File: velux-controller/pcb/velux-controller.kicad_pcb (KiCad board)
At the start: 2 copper layers, 69.9 x 69.8 mm, 35 parts, among them J1 UART, J2 POWER, J3 SIGNAL, J4 PWR, Q1 MMBT3904, Q2 MMBT3904, Q3 MMBT3904, SW1 BOOT, SW2 RST, U1 ESP-12F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

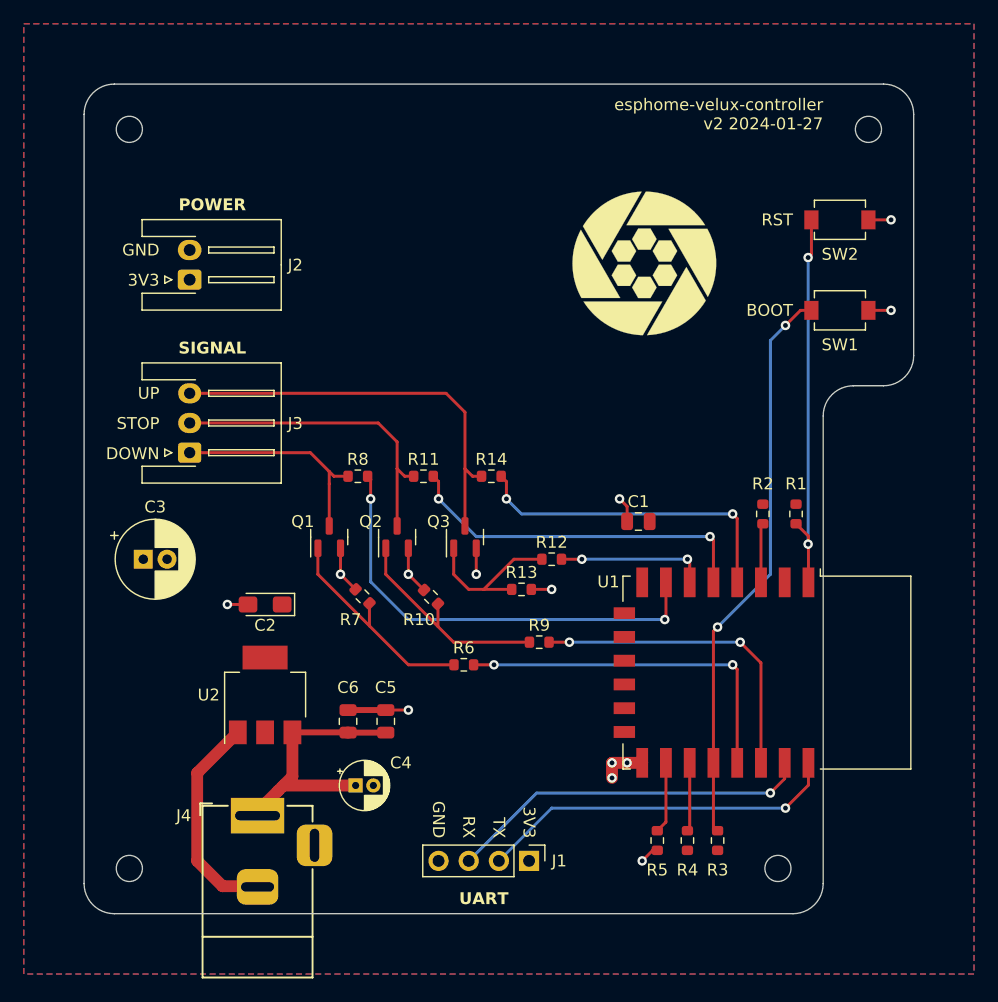
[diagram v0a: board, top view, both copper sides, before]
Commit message: Removing other files that aren't changed. Updated Velux
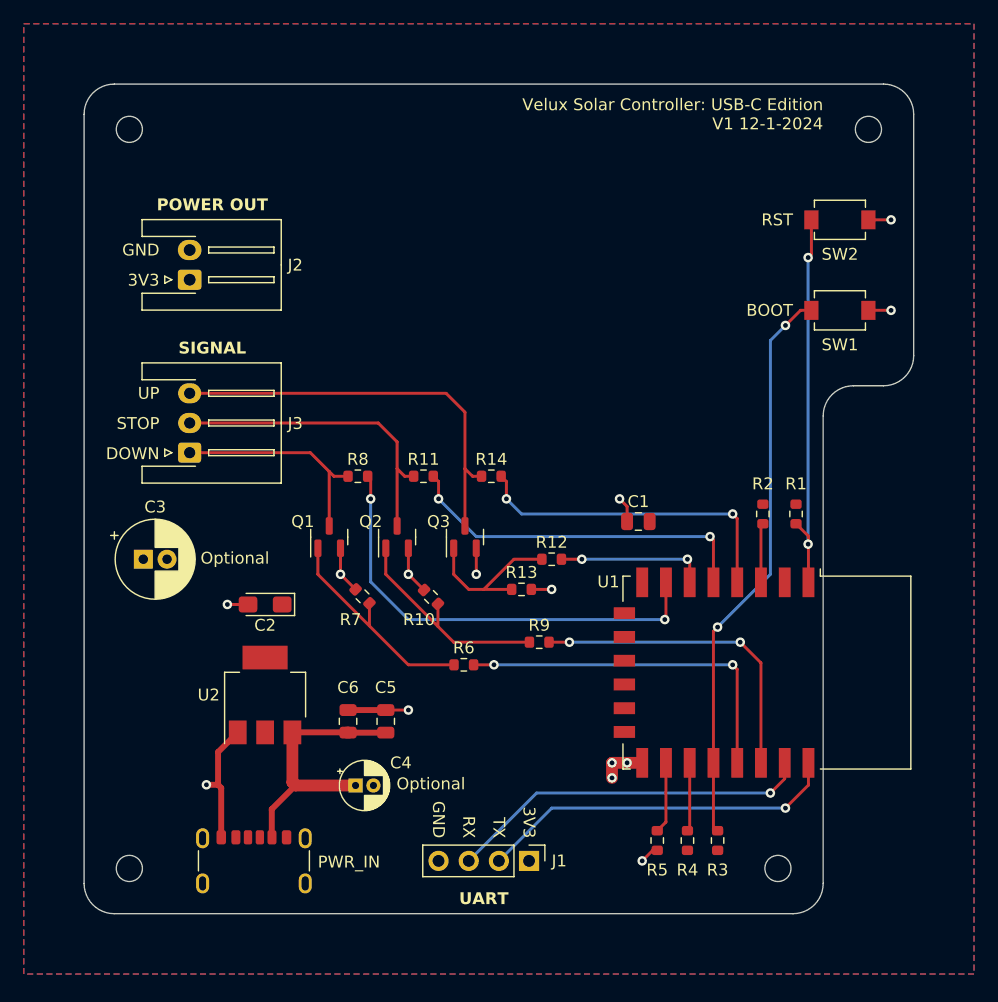
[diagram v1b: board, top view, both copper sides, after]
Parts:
- removed J4: PWR, footprints:DC_barrel_jack_2.1mm
- added PWR_IN: USB_C_Receptacle_GCT_USB4125-xx-x_6P_TopMnt_Horizontal, Connector_USB:USB_C_Receptacle_GCT_USB4125-xx-x_6P_TopMnt_Horizontal, F.Cu at (154.0, 130.0)
- J2: value POWER -> POWER OUT
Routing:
- net GND: track 48.4 -> 40.8 mm, vias 13 -> 14
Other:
- board text added: "Optional"
- board text added: "Velux Solar Controller: USB-C Edition V1 12-1-2024"
- board text removed: "JLCJLCJLCJLC"
- board text removed: "esphome-velux-controller v2 2024-01-27"
